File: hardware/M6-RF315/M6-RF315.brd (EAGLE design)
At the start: 90 x 56 mm, 42 parts, among them J1 CON-71439-2164, J2 CON-SMA-VERT, M1 MOUNT-HOLE3.3, M2 MOUNT-HOLE3.3, M3 MOUNT-HOLE3.3, M4 MOUNT-HOLE3.3, M5 FIDUCIAL1X2, M6 FIDUCIAL1X2, M7 FIDUCIAL1X2, M8 FIDUCIAL1X2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

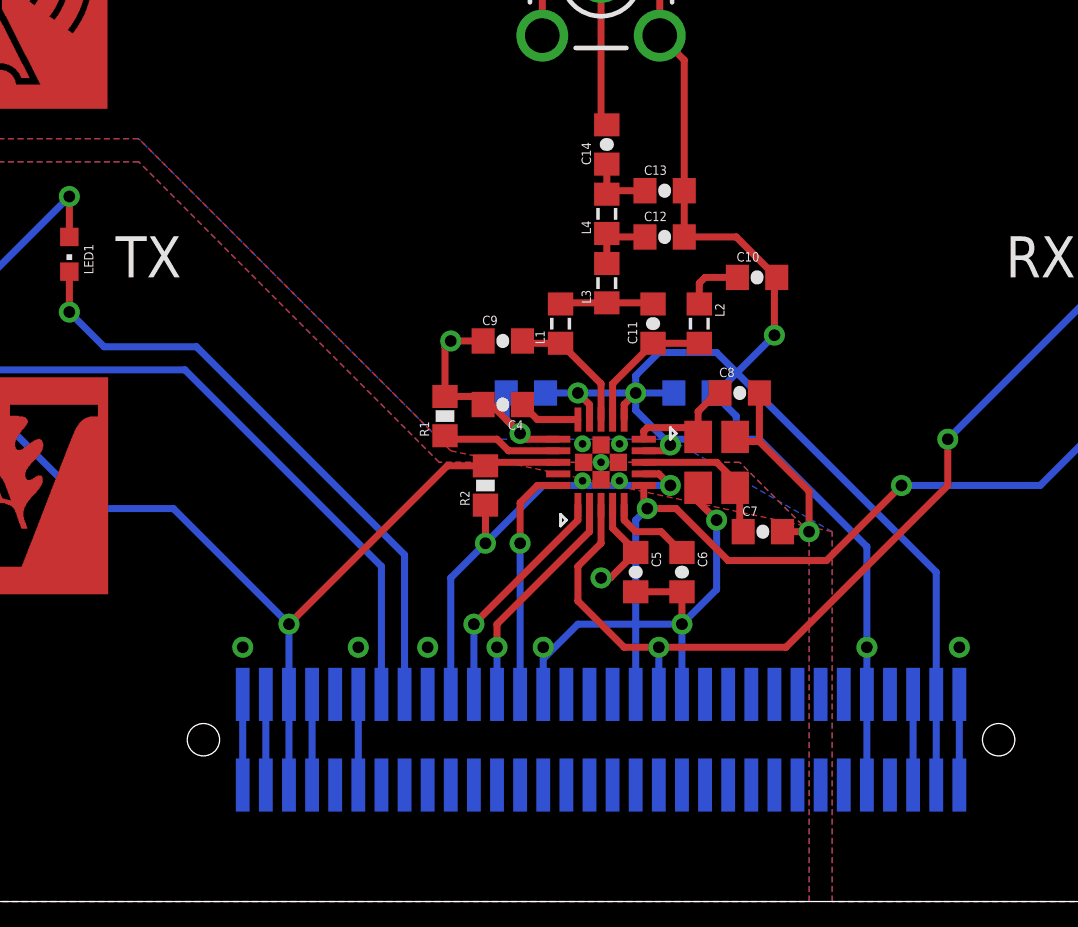
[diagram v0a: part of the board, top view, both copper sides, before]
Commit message: All signals routed on M6-RF315. Needs DRC check.
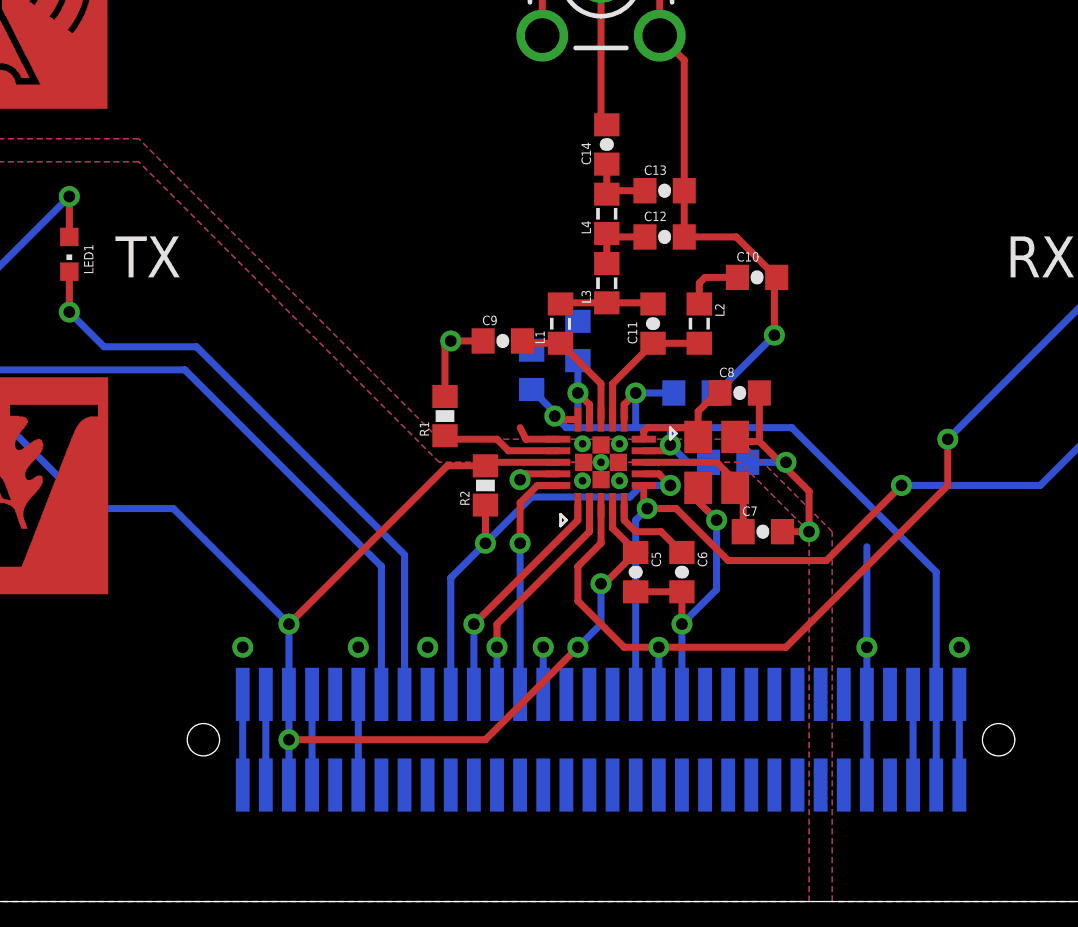
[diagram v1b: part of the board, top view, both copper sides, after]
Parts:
- moved C3 3.18 mm to (44.0, 24.2), turned to 90 degrees
- moved C4 1.95 mm to (42.0, 23.0), flipped to the bottom, turned to 90 degrees
- moved C1 1.12 mm to (50.5, 19.0)
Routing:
- net D3V3: track 53.1 -> 70.5 mm, vias 2 -> 4
- net AGND: track 71.1 -> 57.4 mm
- net DGND: track 38.5 -> 34.1 mm, vias 7 -> 8
- net A3V3: track 43.5 -> 43.9 mm, vias 3 -> 4

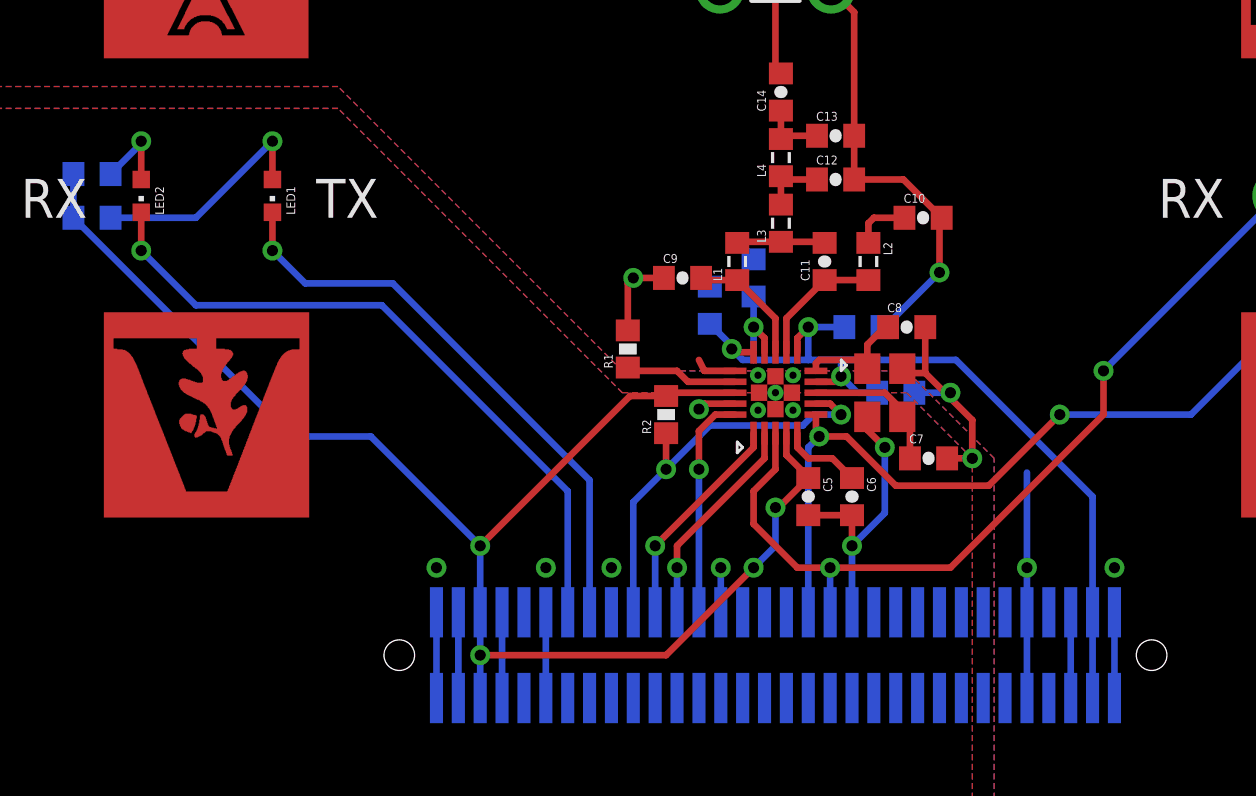
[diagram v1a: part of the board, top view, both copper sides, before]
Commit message: Added a BOM file (not finished yet).
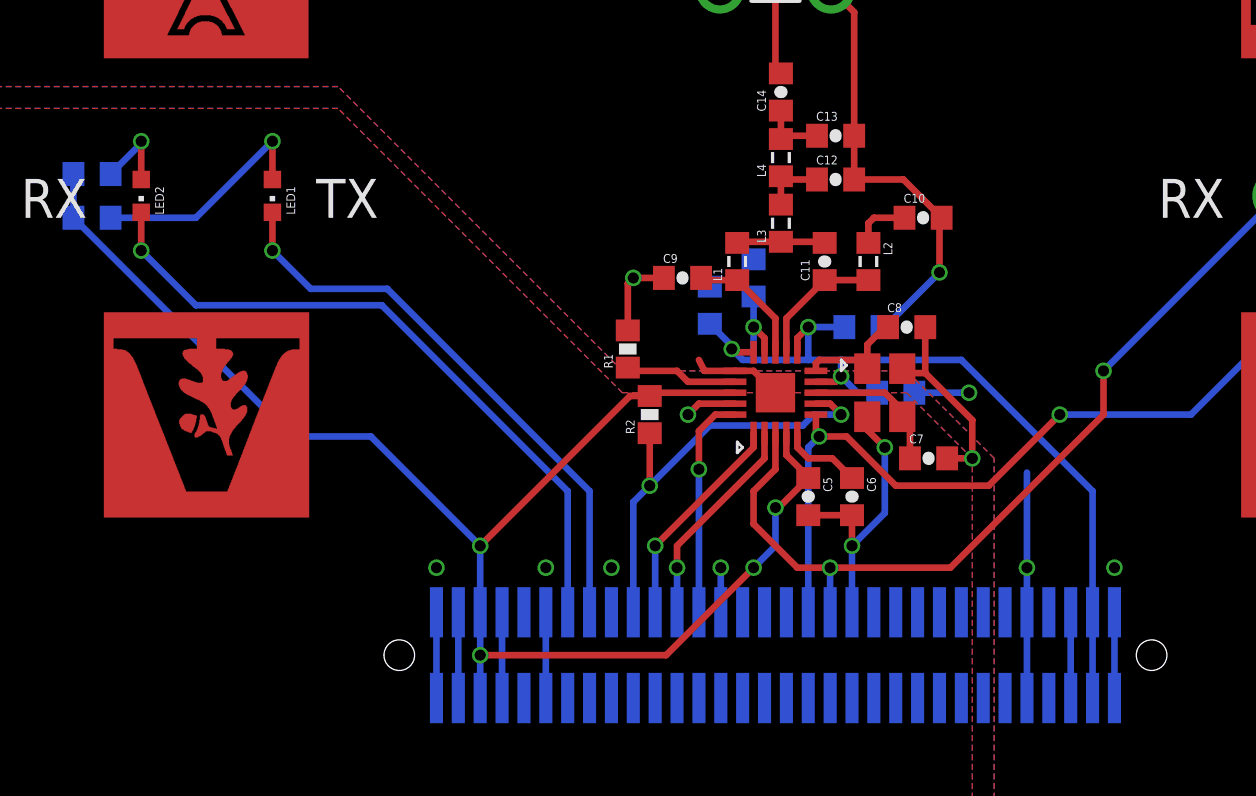
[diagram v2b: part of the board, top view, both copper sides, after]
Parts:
- C9: value 6.8 pF -> 6.8pF
- moved R2 0.75 mm to (39.2, 18.0)
- renumbered U$3 to LOGO4
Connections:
- net AGND: now also U1.EXP
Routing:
- net AGND: track 57.4 -> 60.5 mm
- net SPI1_NSS: track 19.2 -> 20.0 mm
- net DGND: track 34.1 -> 34.7 mm

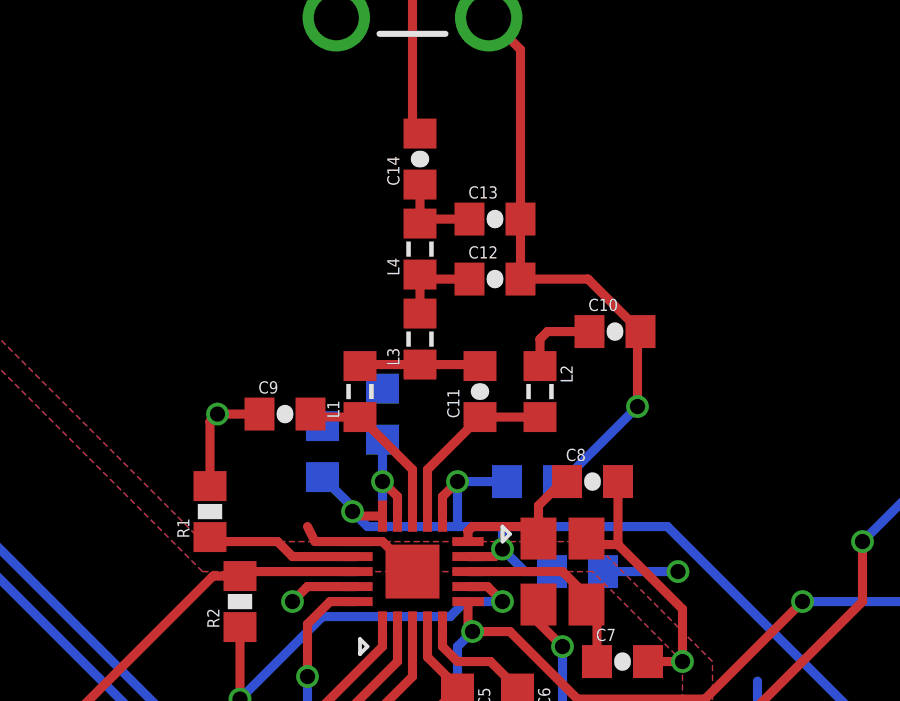
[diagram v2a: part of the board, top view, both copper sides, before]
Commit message: Finished BOM file for M6-RF315.
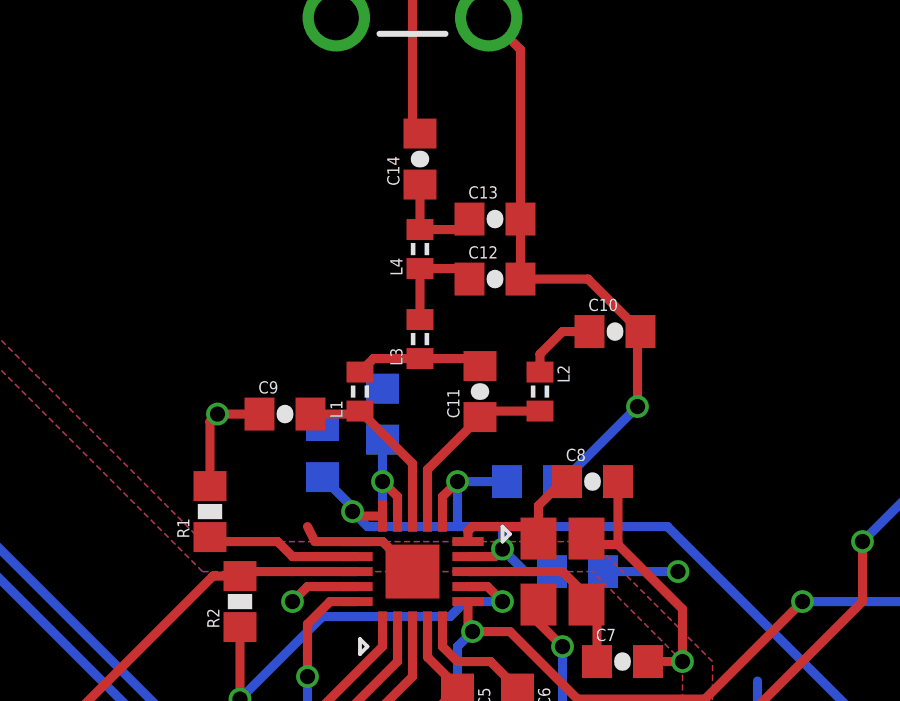
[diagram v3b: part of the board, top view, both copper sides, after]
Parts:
- L1, L2, L3, L4: device M6-RF315:L0603 -> M6-RF315:L0402
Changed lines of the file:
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@@
 <setting verticaltext="up"/>
 </settings>
-<grid distance="1" unitdist="mm" unit="mm" style="lines" multiple="1" display="yes" altdistance="0.1" altunitdist="mm" altunit="mm"/>
+<grid distance="1" unitdist="mm" unit="mm" style="lines" multiple="1" display="yes" altdistance="0.5" altunitdist="mm" altunit="mm"/>
 <layers>
 <layer number="1" name="Top" color="4" fill="1" visible="yes" active="yes"/>
@@
 <layer number="14" name="Route14" color="1" fill="6" visible="no" active="no"/>
 <layer number="15" name="Route15" color="4" fill="6" visible="no" active="no"/>
-<layer number="16" name="Bottom" color="1" fill="1" visible="yes" active="yes"/>
+<layer number="16" name="Bottom" color="1" fill="1" visible="no" active="yes"/>
 <layer number="17" name="Pads" color="2" fill="1" visible="yes" active="yes"/>
 <layer number="18" name="Vias" color="2" fill="1" visible="yes" active="yes"/>
@@
 <layer number="20" name="Dimension" color="15" fill="1" visible="yes" active="yes"/>
 <layer number="21" name="tPlace" color="7" fill="1" visible="yes" active="yes"/>
-<layer number="22" name="bPlace" color="7" fill="1" visible="yes" active="yes"/>
+<layer number="22" name="bPlace" color="7" fill="1" visible="no" active="yes"/>
 <layer number="23" name="tOrigins" color="15" fill="1" visible="yes" active="yes"/>
-<layer number="24" name="bOrigins" color="15" fill="1" visible="yes" active="yes"/>
+<layer number="24" name="bOrigins" color="15" fill="1" visible="no" active="yes"/>
 <layer number="25" name="tNames" color="7" fill="1" visible="yes" active="yes"/>
-<layer number="26" name="bNames" color="7" fill="1" visible="yes" active="yes"/>
+<layer number="26" name="bNames" color="7" fill="1" visible="no" active="yes"/>
 <layer number="27" name="tValues" color="7" fill="1" visible="yes" active="yes"/>
-<layer number="28" name="bValues" color="7" fill="1" visible="yes" active="yes"/>
+<layer number="28" name="bValues" color="7" fill="1" visible="no" active="yes"/>
 <layer number="29" name="tStop" color="7" fill="3" visible="no" active="yes"/>
 <layer number="30" name="bStop" color="7" fill="6" visible="no" active="yes"/>
@@
 <layer number="38" name="bTest" color="7" fill="1" visible="no" active="yes"/>
 <layer number="39" name="tKeepout" color="4" fill="11" visible="yes" active="yes"/>
-<layer number="40" name="bKeepout" color="1" fill="11" visible="yes" active="yes"/>
+<layer number="40" name="bKeepout" color="1" fill="11" visible="no" active="yes"/>
 <layer number="41" name="tRestrict" color="4" fill="10" visible="yes" active="yes"/>
-<layer number="42" name="bRestrict" color="1" fill="10" visible="yes" active="yes"/>
+<layer number="42" name="bRestrict" color="1" fill="10" visible="no" active="yes"/>
 <layer number="43" name="vRestrict" color="2" fill="10" visible="yes" active="yes"/>
 <layer number="44" name="Drills" color="7" fill="1" visible="no" active="yes"/>
@@
 <layer number="50" name="dxf" color="7" fill="1" visible="no" active="no"/>
 <layer number="51" name="tDocu" color="7" fill="1" visible="yes" active="yes"/>
-<layer number="52" name="bDocu" color="7" fill="1" visible="yes" active="yes"/>
+<layer number="52" name="bDocu" color="7" fill="1" visible="no" active="yes"/>
 <layer number="53" name="tGND_GNDA" color="7" fill="9" visible="no" active="no"/>
 <layer number="54" name="bGND_GNDA" color="1" fill="9" visible="no" active="no"/>
@@
 <attribute name="FUNCTION" value="RF LC filter DC blocking capacitor" x="45.25" y="32.75" size="1.778" layer="27" rot="R90" display="off"/>
 </element>
-<element name="L1" library="M6-RF315" package="L0603" value="33nH" x="43.25" y="25" rot="R90">
+<element name="L1" library="M6-RF315" package="L0402" value="33nH" x="43.25" y="25" rot="R90">
 <attribute name="FUNCTION" value="RF balun/matching inductor" x="43.25" y="25" size="1.778" layer="27" rot="R90" display="off"/>
 </element>
-<element name="L2" library="M6-RF315" package="L0603" value="33nH" x="49.25" y="25" rot="R270">
+<element name="L2" library="M6-RF315" package="L0402" value="33nH" x="49.25" y="25" rot="R270">
 <attribute name="FUNCTION" value="RF balun/matching inductor" x="49.25" y="25" size="1.778" layer="27" rot="R270" display="off"/>
 </element>
-<element name="L3" library="M6-RF315" package="L0603" value="18nH" x="45.25" y="26.75" rot="R90">
+<element name="L3" library="M6-RF315" package="L0402" value="18nH" x="45.25" y="26.75" rot="R90">
 <attribute name="FUNCTION" value="RF LC filter/matching filter inductor" x="45.25" y="26.75" size="1.778" layer="27" rot="R90" display="off"/>
 </element>
-<element name="L4" library="M6-RF315" package="L0603" value="33nH" x="45.25" y="29.75" rot="R90">
+<element name="L4" library="M6-RF315" package="L0402" value="33nH" x="45.25" y="29.75" rot="R90">
 <attribute name="FUNCTION" value="RF LC filter/matching filter inductor" x="45.25" y="29.75" size="1.778" layer="27" rot="R90" display="off"/>
 </element>
@@
 <wire x1="45.5" y1="20.85" x2="45.5" y2="22.4" width="0.3048" layer="1"/>
 <wire x1="45.5" y1="22.4" x2="47.25" y2="24.15" width="0.3048" layer="1"/>
-<wire x1="49.25" y1="24.15" x2="47.25" y2="24.15" width="0.3048" layer="1"/>
+<wire x1="49.25" y1="24.35" x2="47.45" y2="24.35" width="0.3048" layer="1"/>
+<wire x1="47.45" y1="24.35" x2="47.25" y2="24.15" width="0.3048" layer="1"/>
 </signal>
 <signal name="N$9">
@@
 <contactref element="C9" pad="2"/>
 <contactref element="L1" pad="1"/>
-<wire x1="45" y1="20.85" x2="45" y2="22.4" width="0.3048" layer="1"/>
-<wire x1="41.6" y1="24.25" x2="41.7" y2="24.15" width="0.3048" layer="1"/>
-<wire x1="41.7" y1="24.15" x2="43.25" y2="24.15" width="0.3048" layer="1"/>
-<wire x1="45" y1="22.4" x2="43.25" y2="24.15" width="0.3048" layer="1"/>
+<wire x1="45" y1="20.85" x2="45" y2="22" width="0.3048" layer="1"/>
+<wire x1="45" y1="22" x2="45" y2="22.4" width="0.3048" layer="1"/>
+<wire x1="43.25" y1="24.35" x2="43.15" y2="24.25" width="0.3048" layer="1"/>
+<wire x1="43.15" y1="24.25" x2="41.6" y2="24.25" width="0.3048" layer="1"/>
+<wire x1="43.25" y1="24.35" x2="45" y2="22.6" width="0.3048" layer="1"/>
+<wire x1="45" y1="22.6" x2="45" y2="22.4" width="0.3048" layer="1"/>
 </signal>
 <signal name="N$10">
@@
 <contactref element="C11" pad="2"/>
 <contactref element="L3" pad="1"/>
-<wire x1="43.25" y1="25.85" x2="43.3" y2="25.9" width="0.3048" layer="1"/>
-<wire x1="43.3" y1="25.9" x2="45.25" y2="25.9" width="0.3048" layer="1"/>
-<wire x1="47.25" y1="25.85" x2="47.2" y2="25.9" width="0.3048" layer="1"/>
-<wire x1="47.2" y1="25.9" x2="45.25" y2="25.9" width="0.3048" layer="1"/>
+<wire x1="45.25" y1="26.1" x2="43.7" y2="26.1" width="0.3048" layer="1"/>
+<wire x1="43.7" y1="26.1" x2="43.25" y2="25.65" width="0.3048" layer="1"/>
+<wire x1="45.25" y1="26.1" x2="47" y2="26.1" width="0.3048" layer="1"/>
+<wire x1="47" y1="26.1" x2="47.25" y2="25.85" width="0.3048" layer="1"/>
 </signal>
 <signal name="N$13">
 <contactref element="L2" pad="1"/>
 <contactref element="C10" pad="1"/>
-<wire x1="49.25" y1="25.85" x2="49.25" y2="26.75" width="0.3048" layer="1"/>
-<wire x1="49.25" y1="26.75" x2="49.5" y2="27" width="0.3048" layer="1"/>
-<wire x1="49.5" y1="27" x2="50.9" y2="27" width="0.3048" layer="1"/>
 <wire x1="51" y1="27" x2="50.9" y2="27" width="0.3048" layer="1"/>
+<wire x1="49.25" y1="25.65" x2="49.25" y2="26.25" width="0.3048" layer="1"/>
+<wire x1="49.25" y1="26.25" x2="50" y2="27" width="0.3048" layer="1"/>
+<wire x1="50" y1="27" x2="50.9" y2="27" width="0.3048" layer="1"/>
 </signal>
 <signal name="N$2">
@@
 <contactref element="L3" pad="2"/>
 <contactref element="L4" pad="1"/>
-<wire x1="45.25" y1="27.6" x2="45.25" y2="28.9" width="0.3048" layer="1"/>
-<wire x1="46.9" y1="28.75" x2="45.4" y2="28.75" width="0.3048" layer="1"/>
-<wire x1="45.4" y1="28.75" x2="45.25" y2="28.9" width="0.3048" layer="1"/>
+<wire x1="45.25" y1="27.4" x2="45.25" y2="29.1" width="0.3048" layer="1"/>
+<wire x1="46.9" y1="28.75" x2="46.55" y2="29.1" width="0.3048" layer="1"/>
+<wire x1="46.55" y1="29.1" x2="45.25" y2="29.1" width="0.3048" layer="1"/>
 </signal>
 <signal name="N$11">
@@
 <contactref element="C14" pad="1"/>
 <contactref element="C13" pad="1"/>
-<wire x1="45.25" y1="31.9" x2="45.25" y2="30.6" width="0.3048" layer="1"/>
-<wire x1="45.25" y1="30.6" x2="45.4" y2="30.75" width="0.3048" layer="1"/>
-<wire x1="45.4" y1="30.75" x2="46.9" y2="30.75" width="0.3048" layer="1"/>
+<wire x1="45.25" y1="31.9" x2="45.25" y2="30.4" width="0.3048" layer="1"/>
+<wire x1="46.9" y1="30.75" x2="46.55" y2="30.4" width="0.3048" layer="1"/>
+<wire x1="46.55" y1="30.4" x2="45.25" y2="30.4" width="0.3048" layer="1"/>
 </signal>
 <signal name="N$12">
